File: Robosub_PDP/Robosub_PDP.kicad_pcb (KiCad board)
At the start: 2 copper layers, 40 x 75 mm, 7 parts, among them J1 Screw_Terminal_01x10, J2 Screw_Terminal_01x10, J3 Conn_01x02_Pin, J4 Conn_01x02_Pin, J5 Conn_01x02_Pin

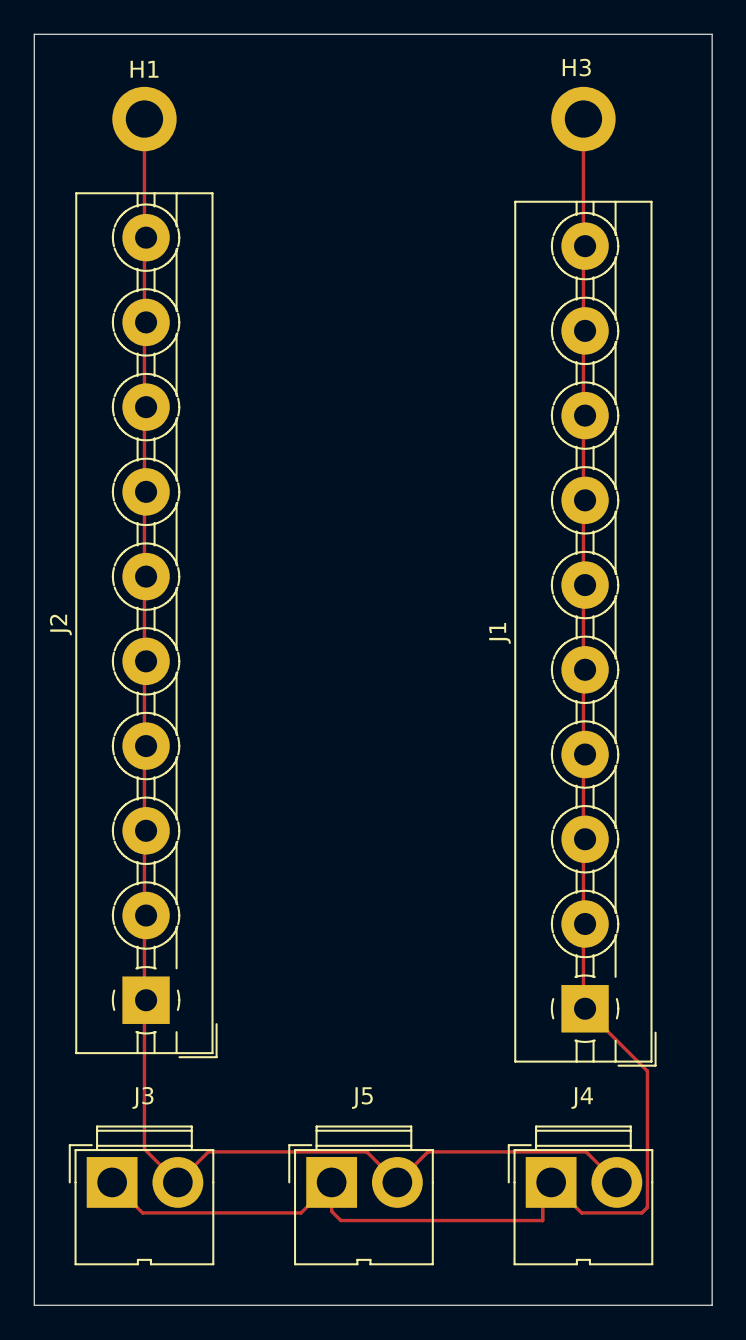
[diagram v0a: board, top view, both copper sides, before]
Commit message: edited errors and added logo
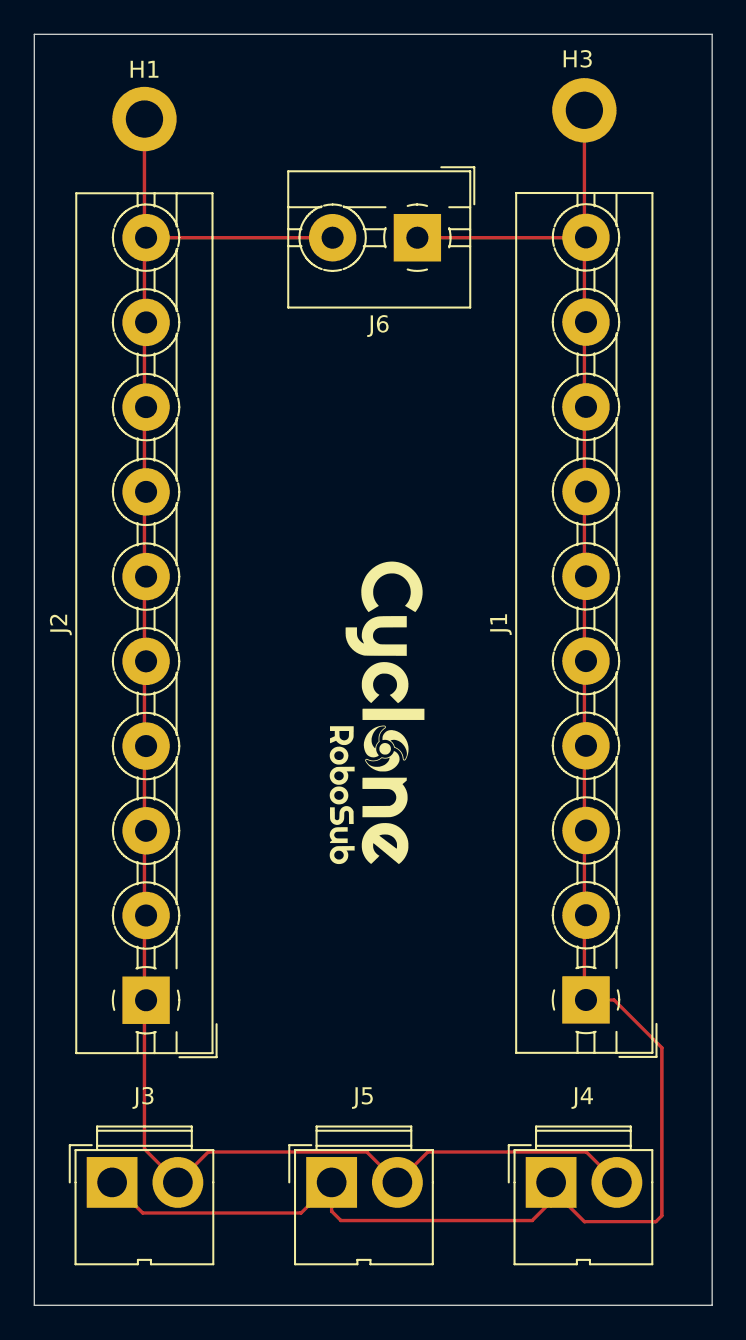
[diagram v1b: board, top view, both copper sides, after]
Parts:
- added G***: LOGO, Graphics:Cyclone_footprint, F.Cu at (194.6, 98.1)
- added J6: Screw_Terminal_01x02, TerminalBlock:TerminalBlock_MaiXu_MX126-5.0-02P_1x02_P5.00mm, F.Cu at (197.1, 70.0)
- moved J1 0.52 mm to (207.1, 115.0)
- moved H3 0.52 mm to (207.0, 62.5)
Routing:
- net Net-(J1-Pin_1): track 103.6 -> 119.3 mm
- net Net-(J2-Pin_1): track 92.5 -> 103.5 mm
